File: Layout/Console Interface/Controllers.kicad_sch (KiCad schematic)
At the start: 12 parts, among them J2 Controller 1, J3 Controller 3, J4 Controller 2, J5 Controller 4

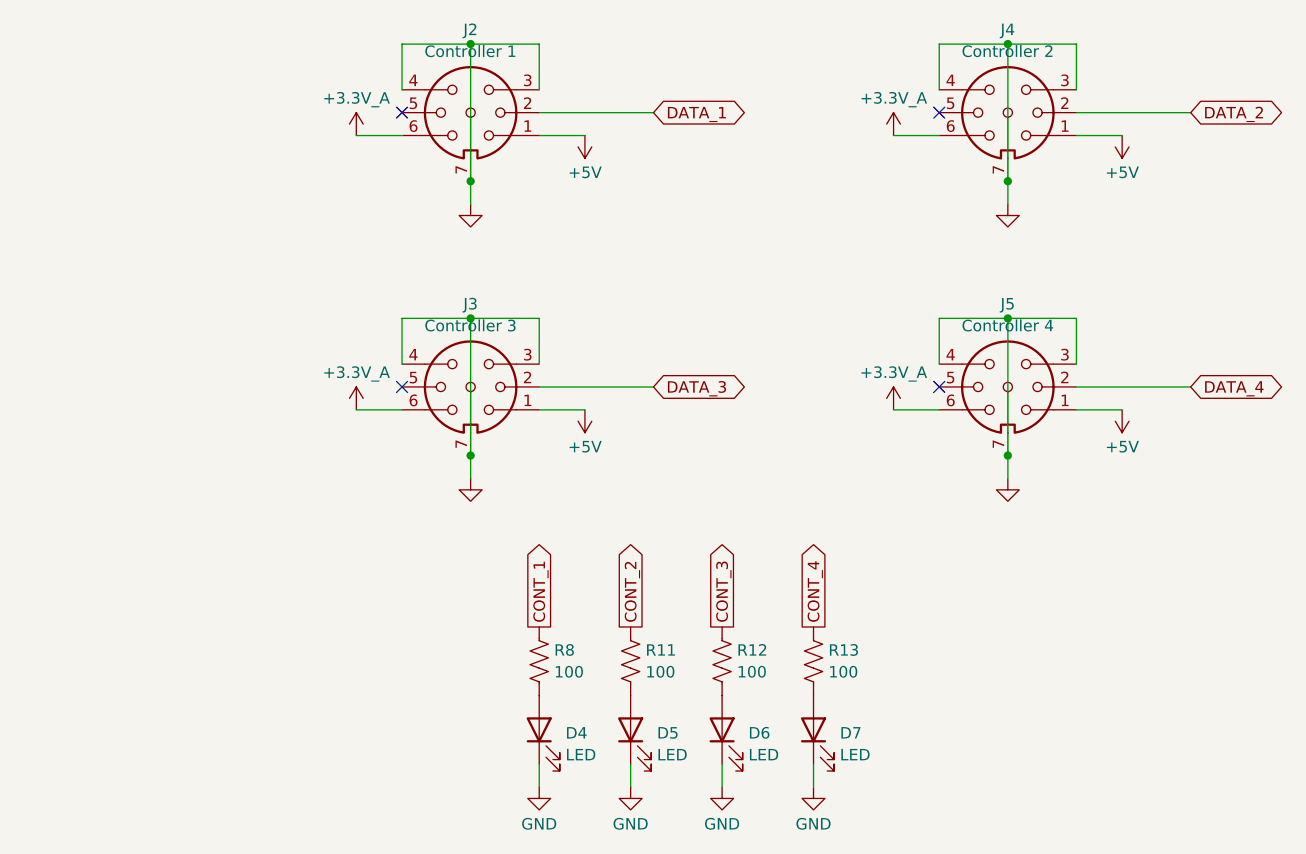
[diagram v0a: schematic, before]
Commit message: Create new footprint for plug clamp
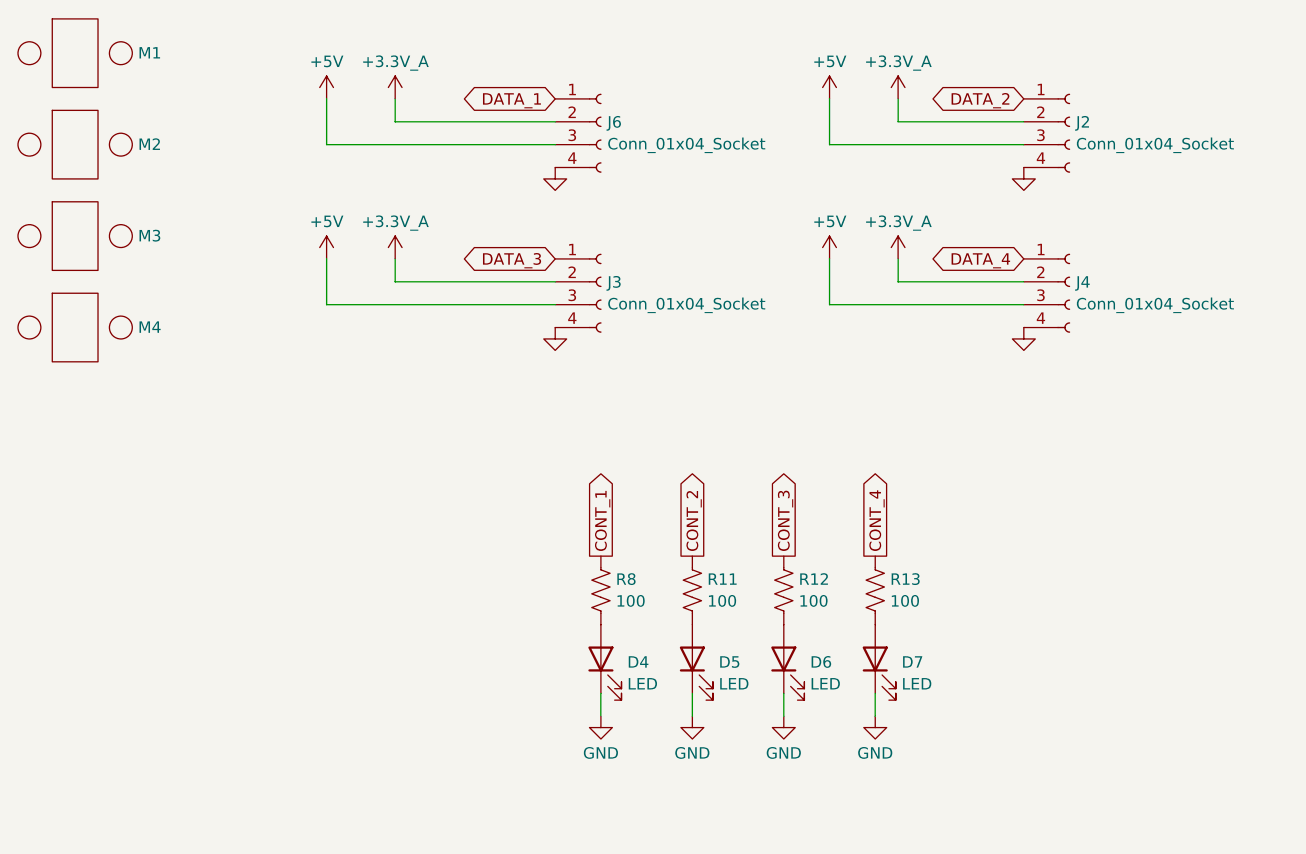
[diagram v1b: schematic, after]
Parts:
- removed J2: Controller 1, GameCube Controllers:Gamecube Controller Socket, symbol Connector:DIN-7_CenterPin7
- removed J3: Controller 3, GameCube Controllers:Gamecube Controller Socket, symbol Connector:DIN-7_CenterPin7
- removed J4: Controller 2, GameCube Controllers:Gamecube Controller Socket, symbol Connector:DIN-7_CenterPin7
- removed J5: Controller 4, GameCube Controllers:Gamecube Controller Socket, symbol Connector:DIN-7_CenterPin7
- added J2, J3, J4, J6: Conn_01x04_Socket, Connector_JST:JST_PH_S4B-PH-SM4-TB_1x04-1MP_P2.00mm_Horizontal, symbol Connector:Conn_01x04_Socket
- added M1, M2, M3, M4: ~, GameCube Controllers:Controller Plug Clamp, symbol GameCube Controllers:Controller_Plug_Clamp
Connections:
- net +3.3V_A: now also J2.2 (Pin_2), J3.2 (Pin_2), J4.2 (Pin_2), J6.2 (Pin_2)
- net +5V: now also J2.3 (Pin_3), J3.3 (Pin_3), J4.3 (Pin_3), J6.3 (Pin_3)
- net DATA_1: now also J6.1 (Pin_1)
- net DATA_2: now also J2.1 (Pin_1)
- net DATA_3: now also J3.1 (Pin_1)
- net DATA_4: now also J4.1 (Pin_1)
- net GND: now also J2.4 (Pin_4), J3.4 (Pin_4), J4.4 (Pin_4), J6.4 (Pin_4)
- no-connect marks 4 -> 0
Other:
- moved on the sheet: D4, D5, D6, D7, R11, R12, R13, R8

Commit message: Add console interface schematic
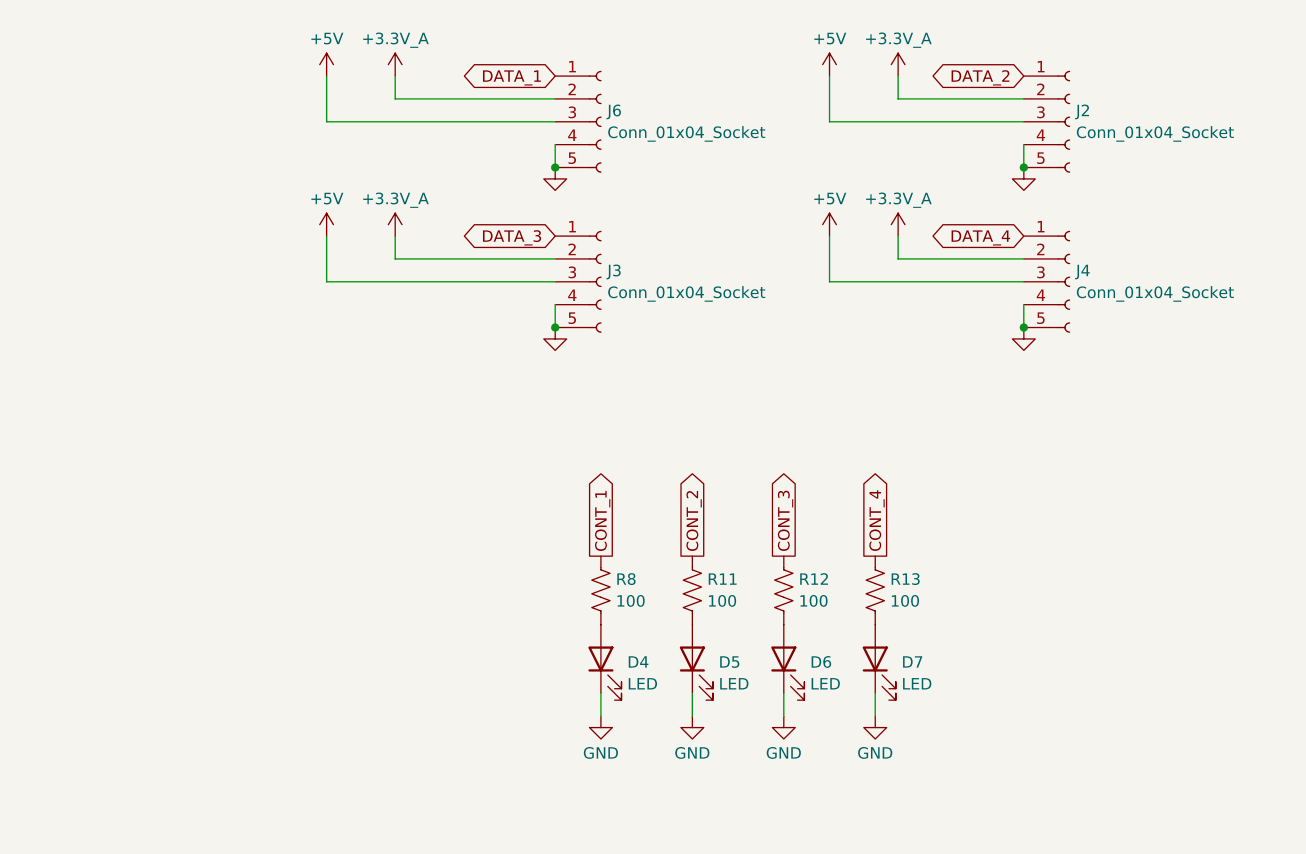
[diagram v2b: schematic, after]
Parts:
- removed M1, M2, M3, M4: ~, GameCube Controllers:Controller Plug Clamp, symbol GameCube Controllers:Controller_Plug_Clamp
- D4, D5, D6, D7: footprint LED_SMD:LED_0805_2012Metric -> LED_SMD:LED_0603_1608Metric
- J2, J3, J4, J6: footprint Connector_JST:JST_PH_S4B-PH-SM4-TB_1x04-1MP_P2.00mm_Horizontal -> Connector_Molex:Molex_Pico-EZmate_78171-0005_1x05-1MP_P1.20mm_Vertical; symbol Connector:Conn_01x04_Socket -> Connector:Conn_01x05_Socket
- R11, R12, R13, R8: footprint Resistor_SMD:R_0805_2012Metric -> Resistor_SMD:R_0603_1608Metric
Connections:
- net GND: now also J2.5 (Pin_5), J3.5 (Pin_5), J4.5 (Pin_5), J6.5 (Pin_5)

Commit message: Use separate board for lights
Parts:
- J2, J3, J4, J6: footprint Connector_Molex:Molex_Pico-EZmate_78171-0005_1x05-1MP_P1.20mm_Vertical -> Connector_JST:JST_GH_BM05B-GHS-TBT_1x05-1MP_P1.25mm_Vertical
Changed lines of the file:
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@@
       (effects (font (size 1.27 1.27)) (justify left))
     )
-    (property "Footprint" "Connector_Molex:Molex_Pico-EZmate_78171-0005_1x05-1MP_P1.20mm_Vertical" (at 125.73 78.74 0)
+    (property "Footprint" "Connector_JST:JST_GH_BM05B-GHS-TBT_1x05-1MP_P1.25mm_Vertical" (at 125.73 78.74 0)
       (effects (font (size 1.27 1.27)) hide)
     )
@@
       (effects (font (size 1.27 1.27)) (justify left))
     )
-    (property "Footprint" "Connector_Molex:Molex_Pico-EZmate_78171-0005_1x05-1MP_P1.20mm_Vertical" (at 125.73 60.96 0)
+    (property "Footprint" "Connector_JST:JST_GH_BM05B-GHS-TBT_1x05-1MP_P1.25mm_Vertical" (at 125.73 60.96 0)
       (effects (font (size 1.27 1.27)) hide)
     )
@@
       (effects (font (size 1.27 1.27)) (justify left))
     )
-    (property "Footprint" "Connector_Molex:Molex_Pico-EZmate_78171-0005_1x05-1MP_P1.20mm_Vertical" (at 177.8 78.74 0)
+    (property "Footprint" "Connector_JST:JST_GH_BM05B-GHS-TBT_1x05-1MP_P1.25mm_Vertical" (at 177.8 78.74 0)
       (effects (font (size 1.27 1.27)) hide)
     )
@@
       (effects (font (size 1.27 1.27)) (justify left))
     )
-    (property "Footprint" "Connector_Molex:Molex_Pico-EZmate_78171-0005_1x05-1MP_P1.20mm_Vertical" (at 177.8 60.96 0)
-      (effects (font (size 1.27 1.27)) hide)
-    )
+    (property "Footprint" "Connector_JST:JST_GH_BM05B-GHS-TBT_1x05-1MP_P1.25mm_Vertical" (at 177.8 60.96 0)
+      (effects (font (size 1.27 1.27)) hide)
+    )
